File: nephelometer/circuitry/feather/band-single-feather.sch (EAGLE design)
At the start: 68 parts, among them IC1 LP2950ACZ-3.3, IC2 LM4041CILP, IC3 AD822N, IC4 7805TV, IC5 MCP6S21, IC6 MAX144, IC7 FEATHER_M0, J1 PJ-102A, J2 MotA, J3 MotA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

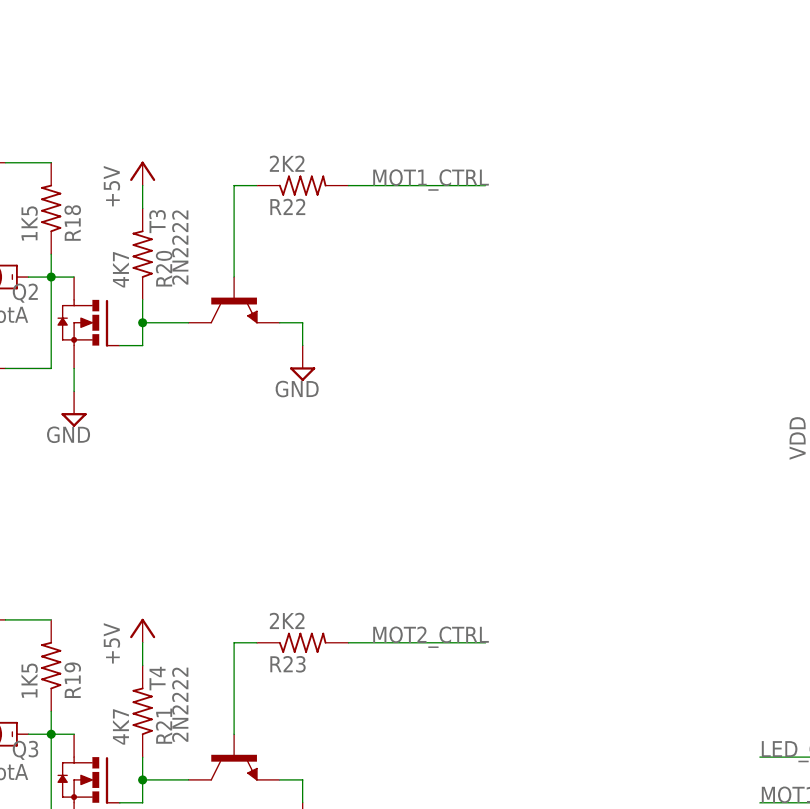
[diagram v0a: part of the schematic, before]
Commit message: Pullup resistor to shut off motors during startup with high-Z pin on microcontroller. Replaced obsolete flyback diode.
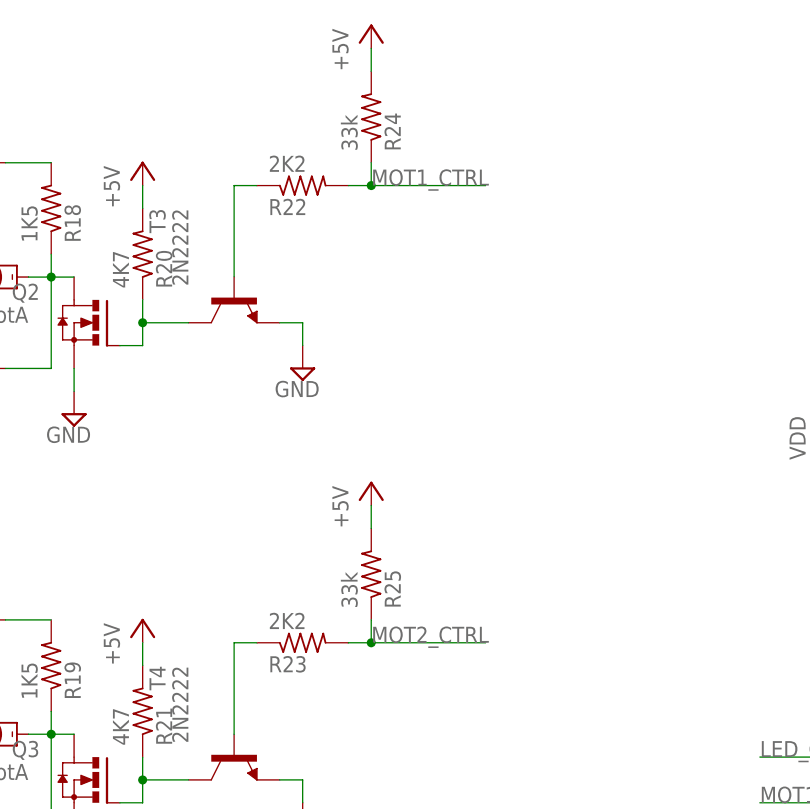
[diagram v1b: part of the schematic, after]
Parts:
- added R24, R25: 33k, adafruit:R-US_0207/9
- D3, D4: DIGIKEY# 1N4935FSCT-ND -> 1N4935GOS-ND; MANF Fairchild Semiconductor -> ON Semiconductor; MANF# 1N4935 -> 1N4935G
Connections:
- net +5V: now also R24.2, R25.2
- net MOT1_CTRL: now also R24.1
- net MOT2_CTRL: now also R25.1
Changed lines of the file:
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@@
 </part>
 <part name="D3" library="adafruit" deviceset="1N4004" device="" value="1N4935">
-<attribute name="DIGIKEY#" value="1N4935FSCT-ND"/>
-<attribute name="MANF" value="Fairchild Semiconductor"/>
-<attribute name="MANF#" value="1N4935"/>
+<attribute name="DIGIKEY#" value="1N4935GOS-ND"/>
+<attribute name="MANF" value="ON Semiconductor"/>
+<attribute name="MANF#" value="1N4935G"/>
 </part>
 <part name="SUPPLY15" library="supply2" deviceset="GND" device=""/>
@@
 </part>
 <part name="D4" library="adafruit" deviceset="1N4004" device="" value="1N4935">
-<attribute name="DIGIKEY#" value="1N4935FSCT-ND"/>
-<attribute name="MANF" value="Fairchild Semiconductor"/>
-<attribute name="MANF#" value="1N4935"/>
+<attribute name="DIGIKEY#" value="1N4935GOS-ND"/>
+<attribute name="MANF" value="ON Semiconductor"/>
+<attribute name="MANF#" value="1N4935G"/>
 </part>
 <part name="SUPPLY16" library="supply2" deviceset="GND" device=""/>
@@
 <attribute name="MANF#" value="FK14X7R1C105K"/>
 </part>
+<part name="R24" library="adafruit" deviceset="R-US_" device="0207/9" value="33k">
+<attribute name="DIGIKEY#" value="CF14JT33K0CT-ND"/>
+<attribute name="MANF" value="Stackpole Electronics Inc"/>
+<attribute name="MANF#" value="CF14JT33K0"/>
+</part>
+<part name="P+11" library="supply1" deviceset="+5V" device=""/>
+<part name="R25" library="adafruit" deviceset="R-US_" device="0207/9" value="33k">
+<attribute name="DIGIKEY#" value="CF14JT33K0CT-ND"/>
+<attribute name="MANF" value="Stackpole Electronics Inc"/>
+<attribute name="MANF#" value="CF14JT33K0"/>
+</part>
+<part name="P+12" library="supply1" deviceset="+5V" device=""/>
 </parts>
 <sheets>
@@
 <attribute name="MANF#" x="185.42" y="106.68" size="1.778" layer="96" display="off"/>
 </instance>
+<instance part="R24" gate="G$1" x="309.88" y="187.96" rot="MR90">
+<attribute name="DIGIKEY#" x="309.88" y="187.96" size="1.778" layer="96" rot="MR90" display="off"/>
+<attribute name="MANF" x="309.88" y="187.96" size="1.778" layer="96" rot="MR90" display="off"/>
+<attribute name="MANF#" x="309.88" y="187.96" size="1.778" layer="96" rot="MR90" display="off"/>
+</instance>
+<instance part="P+11" gate="1" x="309.88" y="198.12"/>
+<instance part="R25" gate="G$1" x="309.88" y="137.16" rot="MR90">
+<attribute name="DIGIKEY#" x="309.88" y="137.16" size="1.778" layer="96" rot="MR90" display="off"/>
+<attribute name="MANF" x="309.88" y="137.16" size="1.778" layer="96" rot="MR90" display="off"/>
+<attribute name="MANF#" x="309.88" y="137.16" size="1.778" layer="96" rot="MR90" display="off"/>
+</instance>
+<instance part="P+12" gate="1" x="309.88" y="147.32"/>
 </instances>
 <busses>
@@
 <wire x1="284.48" y1="129.54" x2="284.48" y2="127" width="0.1524" layer="91"/>
 </segment>
+<segment>
+<pinref part="P+11" gate="1" pin="+5V"/>
+<pinref part="R24" gate="G$1" pin="2"/>
+<wire x1="309.88" y1="195.58" x2="309.88" y2="193.04" width="0.1524" layer="91"/>
+</segment>
+<segment>
+<pinref part="P+12" gate="1" pin="+5V"/>
+<pinref part="R25" gate="G$1" pin="2"/>
+<wire x1="309.88" y1="144.78" x2="309.88" y2="142.24" width="0.1524" layer="91"/>
+</segment>
 </net>
 <net name="N$4" class="0">
@@
 <segment>
 <pinref part="R22" gate="G$1" pin="2"/>
-<wire x1="322.58" y1="180.34" x2="307.34" y2="180.34" width="0.1524" layer="91"/>
+<wire x1="322.58" y1="180.34" x2="309.88" y2="180.34" width="0.1524" layer="91"/>
 <label x="309.88" y="180.34" size="1.778" layer="95"/>
+<pinref part="R24" gate="G$1" pin="1"/>
+<wire x1="309.88" y1="180.34" x2="307.34" y2="180.34" width="0.1524" layer="91"/>
+<wire x1="309.88" y1="182.88" x2="309.88" y2="180.34" width="0.1524" layer="91"/>
+<junction x="309.88" y="180.34"/>
 </segment>
 </net>
@@
 <segment>
 <pinref part="R23" gate="G$1" pin="2"/>
-<wire x1="322.58" y1="129.54" x2="307.34" y2="129.54" width="0.1524" layer="91"/>
+<wire x1="322.58" y1="129.54" x2="309.88" y2="129.54" width="0.1524" layer="91"/>
 <label x="309.88" y="129.54" size="1.778" layer="95"/>
-</segment>
-</net>
+<pinref part="R25" gate="G$1" pin="1"/>
+<wire x1="309.88" y1="129.54" x2="307.34" y2="129.54" width="0.1524" layer="91"/>
+<wire x1="309.88" y1="132.08" x2="309.88" y2="129.54" width="0.1524" layer="91"/>
+<junction x="309.88" y="129.54"/>
+</segment>
+</net>
